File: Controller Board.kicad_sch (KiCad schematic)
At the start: 3 parts, among them J1 Conn_01x12_Socket, J2 Conn_01x12_Socket

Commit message: checkpoint
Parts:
- J3: renamed from J1; value Conn_01x12_Socket -> Conn_01x12_Header; footprint Connector_PinSocket_2.54mm:PinSocket_1x12_P2.54mm_Vertical -> Connector_PinHeader_2.54mm:PinHeader_1x12_P2.54mm_Vertical
- J4: renamed from J2; value Conn_01x12_Socket -> Conn_01x12_Header; footprint Connector_PinSocket_2.54mm:PinSocket_1x12_P2.54mm_Vertical -> Connector_PinHeader_2.54mm:PinHeader_1x12_P2.54mm_Vertical
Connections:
- net COL0 renamed _COL0
- net COL1 renamed _COL1
- net COL10 renamed _COL10
- net COL11 renamed _COL11
- net COL12 renamed _COL12
- net COL13 renamed _COL13
- net COL14 renamed _COL14
- net COL15 renamed _COL15
- net COL2 renamed _COL2
- net COL3 renamed _COL3
- net COL4 renamed _COL4
- net COL5 renamed _COL5
- net COL6 renamed _COL6
- net COL7 renamed _COL7
- net COL8 renamed _COL8
- net COL9 renamed _COL9
- net ROW0 renamed _ROW0
- net ROW1 renamed _ROW1
- net ROW2 renamed _ROW2
- net ROW3 renamed _ROW3
- net ROW4 renamed _ROW4
- no-connect marks 0 -> 1

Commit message: checkpoint w gemini routed
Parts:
- added U1: ProMicro, keebio:Elite-C, symbol kbd:ProMicro
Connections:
- net GND: now also U1.23 (GND), U1.3 (GND), U1.4 (GND)
- net VCC: now also U1.21 (VCC)
- net _LEDIN: now reaches J4.3 (Pin_3)
- no-connect marks 1 -> 0

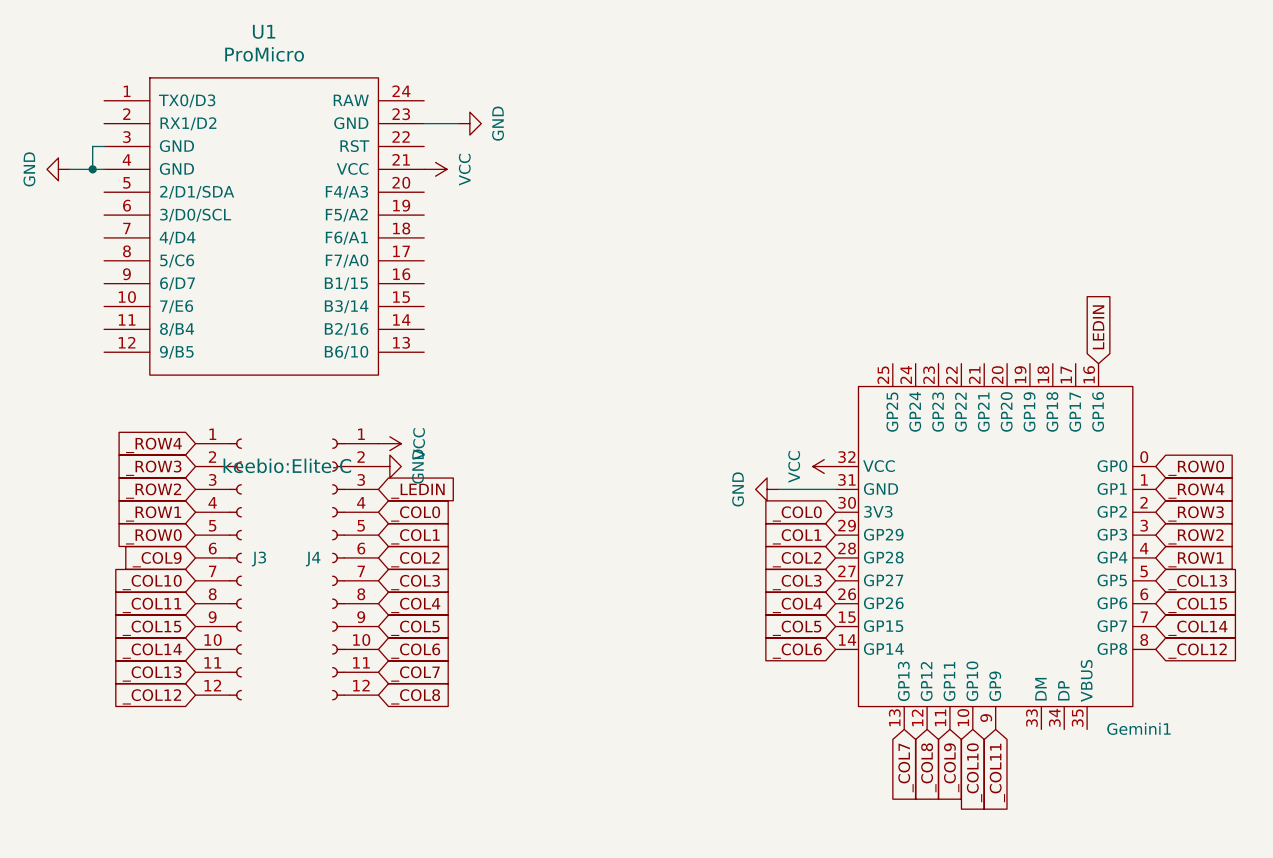
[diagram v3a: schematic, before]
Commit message: use pro micro over gemini
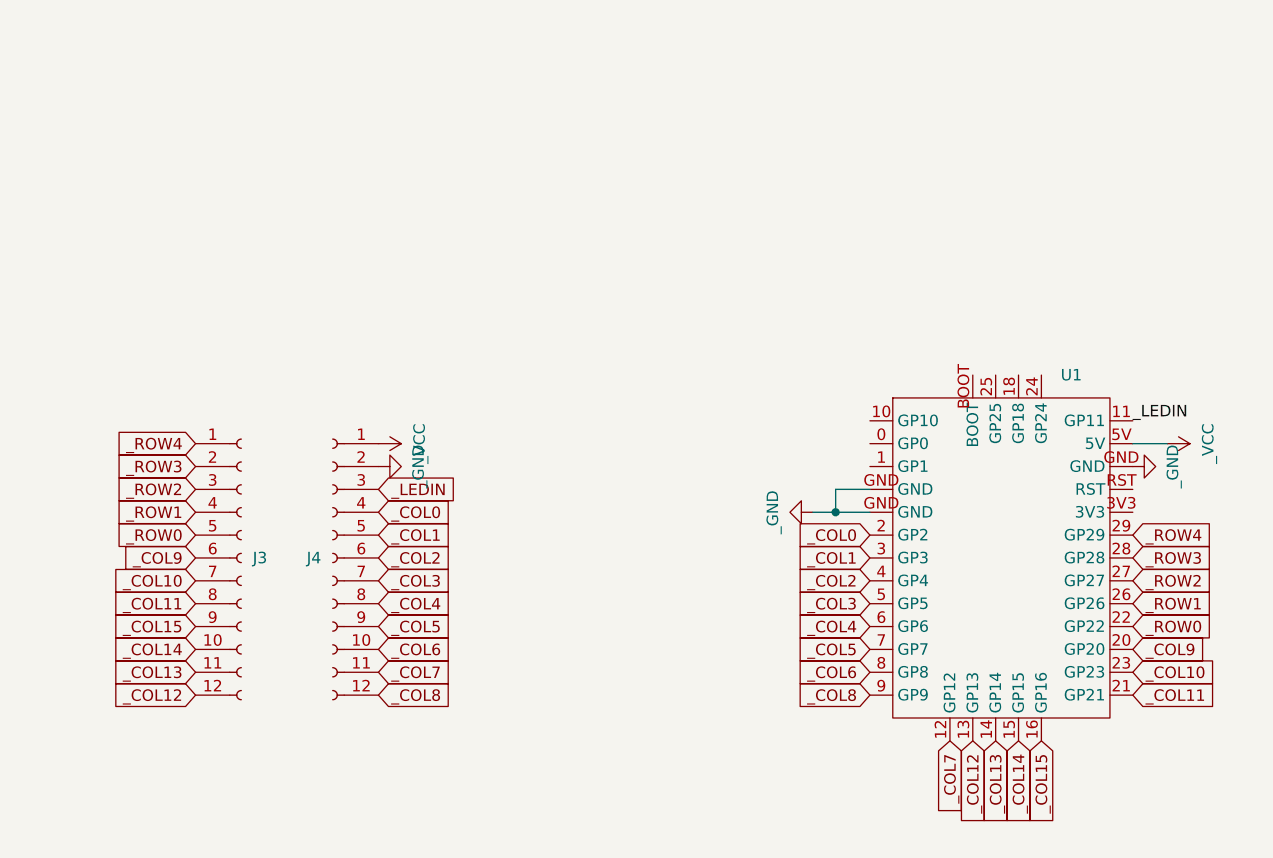
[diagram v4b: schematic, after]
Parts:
- removed U1: ProMicro, keebio:Elite-C, symbol kbd:ProMicro
- U1: renamed from Gemini1; footprint Gemini:gemini -> kicad_pro_micro_rp2040:pro_micro_rp2040; symbol local:gemini -> promicro rp2040:pro_micro_rp2040; now in the parts list
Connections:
- net LEDIN is gone; now on net _COL15: U1.16 (GP16)
- net _COL0: now also U1.2 (GP2); no longer U1.30 (3V3)
- net _COL1: now also U1.3 (GP3); no longer U1.29 (GP29)
- net _COL10: now also U1.23 (GP23); no longer U1.10 (GP10)
- net _COL11: now also U1.21 (GP21); no longer U1.9 (GP9)
- net _COL12: now also U1.13 (GP13); no longer U1.8 (GP8)
- net _COL13: now also U1.14 (GP14); no longer U1.5 (GP5)
- net _COL14: now also U1.15 (GP15); no longer U1.7 (GP7)
- net _COL15: no longer U1.6 (GP6)
- net _COL2: now also U1.4 (GP4); no longer U1.28 (GP28)
- net _COL3: now also U1.5 (GP5); no longer U1.27 (GP27)
- net _COL4: now also U1.6 (GP6); no longer U1.26 (GP26)
- net _COL5: now also U1.7 (GP7); no longer U1.15 (GP15)
- net _COL6: now also U1.8 (GP8); no longer U1.14 (GP14)
- net _COL7: now also U1.12 (GP12); no longer U1.13 (GP13)
- net _COL8: now also U1.9 (GP9); no longer U1.12 (GP12)
- net _COL9: now also U1.20 (GP20); no longer U1.11 (GP11)
- net _LEDIN: now also U1.11 (GP11)
- net _ROW0: now also U1.22 (GP22); no longer U1.0 (GP0)
- net _ROW1: now also U1.26 (GP26); no longer U1.4 (GP4)
- net _ROW2: now also U1.27 (GP27); no longer U1.3 (GP3)
- net _ROW3: now also U1.28 (GP28); no longer U1.2 (GP2)
- net _ROW4: now also U1.29 (GP29); no longer U1.1 (GP1)
- net GND renamed _GND
- net _GND: now also U1.GND; no longer U1.31 (GND)
- net VCC renamed _VCC
- net _VCC: now also U1.5V; no longer U1.32 (VCC)
